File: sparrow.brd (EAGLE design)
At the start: 100 x 100 mm, 189 parts, among them IC1 LAN8720AVIAS, IC2 TLV320AIC3100VIAS, IC3 TPS2500, IC4 SKYWORKS_AAT4280ASC70JW-8-NOT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, IC5 SKYWORKS_AAT4280ASC70JW-8-NOT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, IC6 SKYWORKS_AAT4280ASC70JW-8-NOT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, IC7 SKYWORKS_AAT4280ASC70JW-8-NOT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, IC8 SKYWORKS_AAT4280ASC70JW-8-NOT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, IC9 FXMA10820-DFN, P1 DEBUG, P3 HEADER-1X10ROUND, P4 SD_CARD, X1 ABS07-32768, X2 50MHZ, X3 32.768KHz, Y1 12MHz, Y2 16MHz

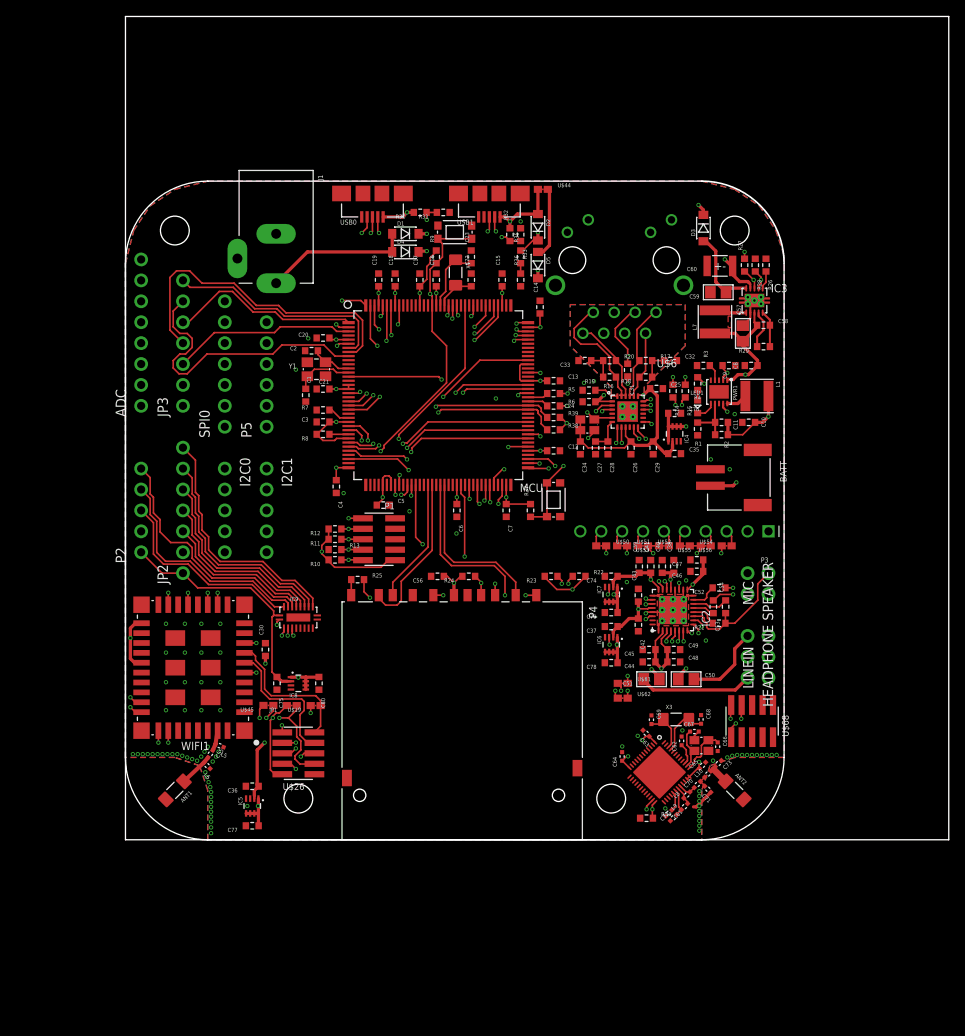
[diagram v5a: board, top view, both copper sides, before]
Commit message: basic routing finished
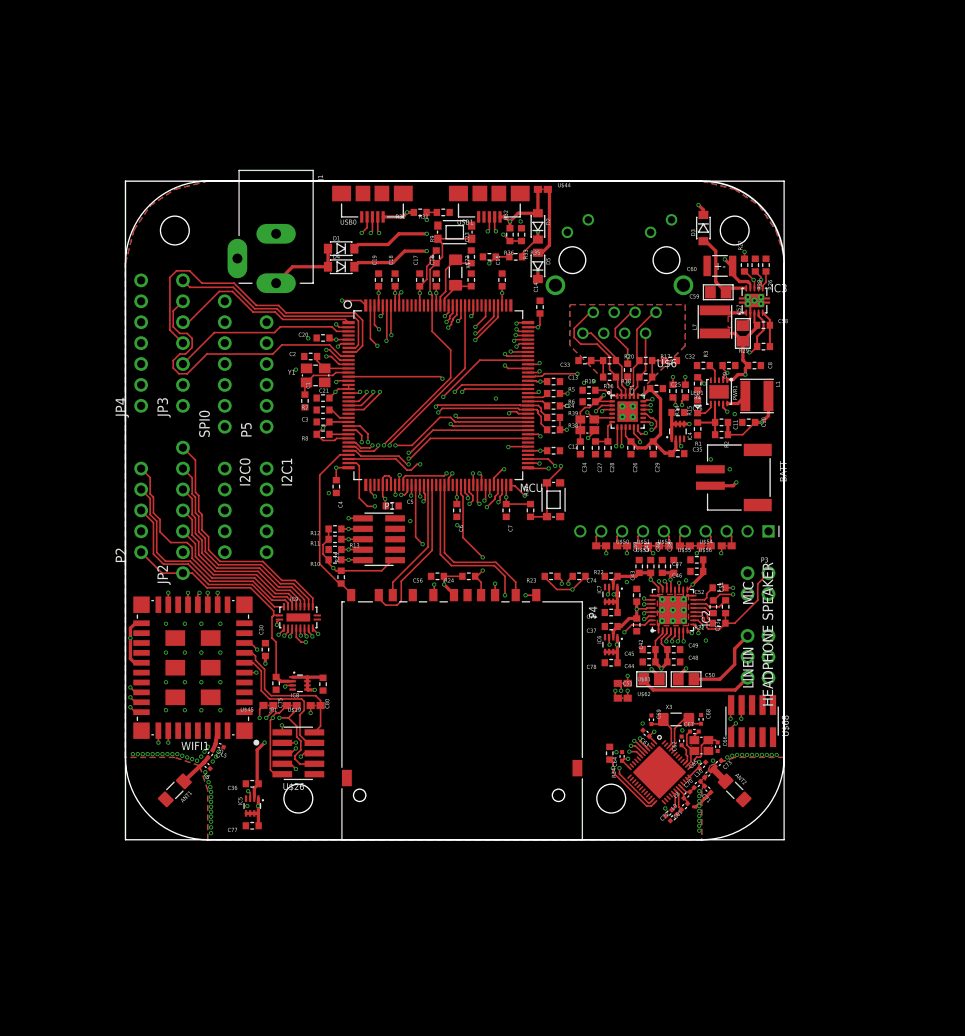
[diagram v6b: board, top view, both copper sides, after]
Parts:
- removed ADC: HEADER-1X8ROUND, anykey:1X08_ROUND
- added JP4: HEADER-1X7ROUND, anykey:1X07_ROUND
- IC3: device anykey:SON10-0.5-EP -> anykey:SON10-0.5-EP-VIAS
- moved R34 9.07 mm to (58.8, 10.5), turned to 270 degrees
- moved D4 8.00 mm to (26.2, 69.6)
- moved D1 8.00 mm to (26.2, 71.8)
- moved R36 4.72 mm to (44.2, 70.8), turned to 0 degrees
- moved R25 2.02 mm to (26.2, 31.9), turned to 90 degrees
- moved C5 1.10 mm to (32.4, 40.5)
- moved C21 1.10 mm to (24.0, 53.6)
- moved Y1 0.76 mm to (23.1, 56.4)
- moved C1 0.71 mm to (21.8, 53.3)
- moved C2 0.71 mm to (22.5, 58.7)
- moved R35 0.60 mm to (47.4, 70.8), turned to 0 degrees
- moved C80 0.51 mm to (24.0, 18.9)
- moved IC4 0.50 mm to (67.1, 49.6)
- moved C76 0.41 mm to (67.1, 51.9)
- moved C8 0.40 mm to (76.4, 57.6), turned to 0 degrees
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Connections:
- removed net ADC7: ADC.8, MCU.136
- new net AVAIL1: MCU.114
- new net AVAIL2: MCU.116
- new net AVAIL6: MCU.117
- new net AVAIL7: MCU.132
- new net AVAIL8: MCU.133
- new net AVAIL9: MCU.134
- net 5V_GEN_EN: now also MCU.95
- net ADC0: now also JP4.1; no longer ADC.1
- net ADC1: now also JP4.2; no longer ADC.2
- net ADC2: now also JP4.3; no longer ADC.3
- net ADC3: now also JP4.4; no longer ADC.4
- net ADC4: now also JP4.5; no longer ADC.5
- net ADC5: now also JP4.6; no longer ADC.6
- net ADC6: now also JP4.7; no longer ADC.7
- net AUDIO_!RESET: now also MCU.121
- net AUDIO_PWR: now also MCU.72
- net ETH_!RST: now also MCU.69
- net ETH_PWR: now also MCU.61
- net GND: now also IC3.EXT1, IC3.EXT2, IC3.EXT3, IC3.EXT4
- net GPIO_1: now also MCU.103
- net GPIO_2: now also MCU.101
- net GPIO_3: now also MCU.100
- net GPIO_4: now also MCU.97
- net GPIO_5: now also MCU.86
- net I2C0_IRQ: now also MCU.11
- net I2C1_IRQ: now also MCU.15
- net NRF_SWDCLK: now also MCU.85
- net NRF_SWDIO: now also MCU.83
- net PORT_PWR_5V: now also MCU.50
- net SD_WP: now also MCU.33
- net SPI0_IRQ: now also MCU.10
- net UART1_CTS: now also MCU1.7
- net UART1_RTS: now also MCU1.6
- net UART1_RXD: now also MCU1.5
- net UART1_TXD: now also MCU1.4
- net V5_IN_SENSE: now also MCU.136
- net WIFI_IRQ: now also MCU.38
- net WIFI_PWR: now also MCU.51
- net WIFI_SW_EN: now also MCU.35
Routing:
- net WIFI_SW_EN: track 0.00 -> 68.5 mm, vias 0 -> 2
- net NRF_SWDCLK: track 25.9 -> 91.9 mm, vias 2 -> 3
- net NRF_SWDIO: track 24.0 -> 85.2 mm, vias 2 -> 3
- net GPIO_1: track 0.00 -> 59.6 mm, vias 0 -> 2
- net AUDIO_!RESET: track 0.00 -> 55.8 mm, vias 0 -> 2
- net GPIO_2: track 0.00 -> 55.6 mm, vias 0 -> 2
- net GPIO_5: track 0.00 -> 55.5 mm, vias 0 -> 2
- net GPIO_3: track 0.00 -> 55.2 mm, vias 0 -> 2
- net GPIO_4: track 0.00 -> 54.4 mm, vias 0 -> 2
- net WIFI_PWR: track 0.00 -> 52.1 mm, vias 0 -> 2
- net UART1_RTS: track 0.00 -> 50.8 mm, vias 0 -> 2
- net ADC7: track 50.6 -> 0.00 mm, vias 1 -> 0
- net UART1_RXD: track 0.00 -> 48.9 mm, vias 0 -> 2
- net UART1_CTS: track 0.00 -> 48.6 mm, vias 0 -> 2
- net UART1_TXD: track 0.00 -> 46.8 mm, vias 0 -> 2
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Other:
- board size 100 x 100 mm -> 80 x 80 mm

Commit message: Silkscreen fixed
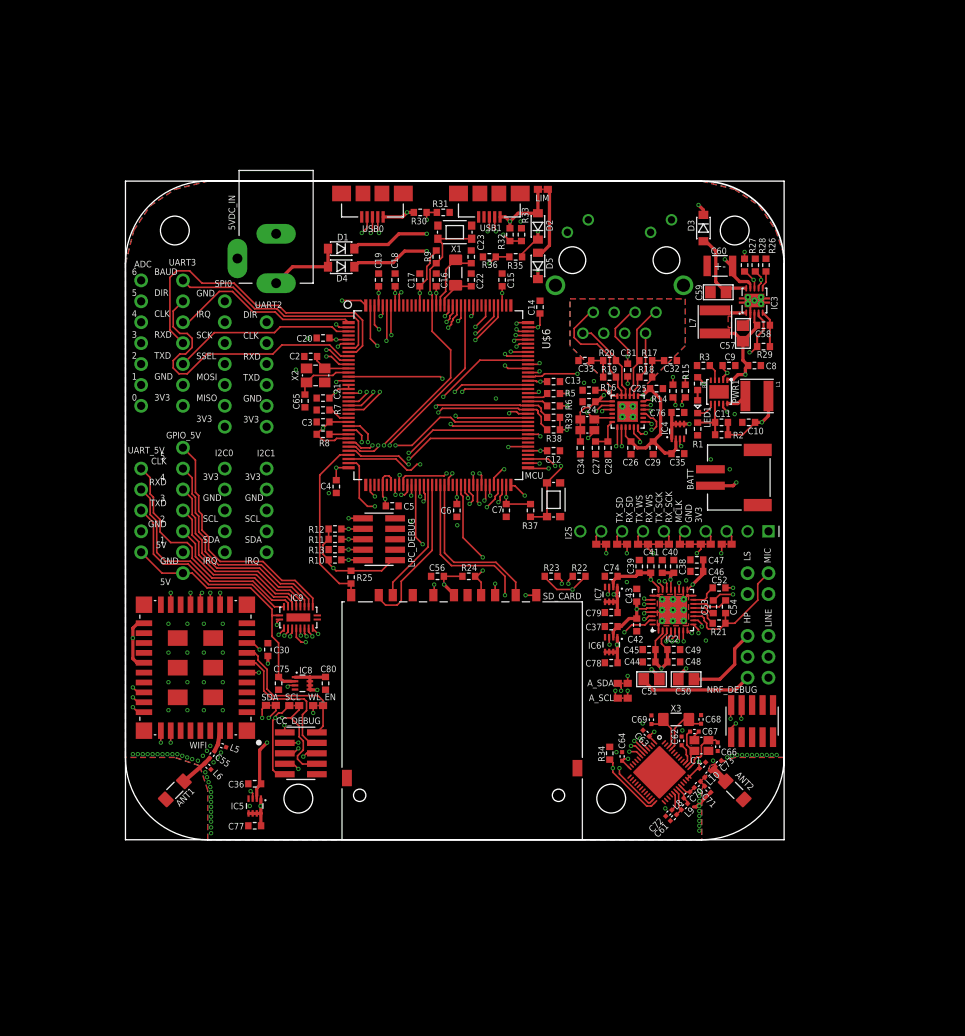
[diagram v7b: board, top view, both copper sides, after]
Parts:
- removed JP1: (no value), anykey:0603_SOLDERJUMPER_CLOSED
- removed U$19, U$45, U$50, U$51, U$52, U$53, U$54, U$55, U$56: JUMPERSOLDER_CLOSED, anykey:0603_SOLDERJUMPER_CLOSED
- removed U$26: HEADER-2X5SMD-1.27MM, anykey:2X05_SMT
- removed WIFI1: CC3000EXTENDED, anykey:CC3000-EXT
- removed Y1: 12MHz, anykey:ABM8G
- added CC_DEBUG: HEADER-2X5SMD-1.27MM, anykey:2X05_SMT
- added LOGO2, LOGO3, LOGO4: LOGOKRONE, anykey:LOGO-KRONE
- added MCLK, RX_SCK, RX_SD, RX_WS, SDA, TX_SCK, TX_SD, TX_WS, WL_EN: JUMPERSOLDER_CLOSED, anykey:0603_SOLDERJUMPER_CLOSED
- added SCL: (no value), anykey:0603_SOLDERJUMPER_CLOSED
- added WIFI: CC3000EXTENDED, anykey:CC3000-EXT
- added X4: 50MHZ, anykey:CRYSTAL25X20
- C1: value 18p -> 1000p; device anykey:0603 -> anykey:0402
- C65: value 1000p -> 18p; device anykey:0402 -> anykey:0603
- X2: value 50MHZ -> 12MHz; device anykey:CRYSTAL25X20 -> anykey:ABM8G
- moved C1 65.5 mm to (70.1, 9.04), turned to 45 degrees
- moved C65 65.5 mm to (21.8, 53.3), turned to 270 degrees
- moved X2 33.5 mm to (23.1, 56.4)
- moved R25 1.20 mm to (27.4, 31.9)
- moved C80 0.32 mm to (24.3, 19.0)
- moved C30 0.30 mm to (17.3, 23.1)
- moved C75 0.30 mm to (18.6, 19.0)
- moved IC8 0.30 mm to (21.5, 19.0)
- moved C36 0.30 mm to (15.7, 6.80)
- moved C77 0.30 mm to (15.7, 1.70)
- moved IC5 0.30 mm to (15.7, 4.10)
- moved L5 0.30 mm to (11.7, 11.4)
- moved C55 0.22 mm to (10.5, 10.3), turned to 235 degrees
- moved L6 0.14 mm to (10.0, 8.92)
- renumbered HEADPHONE to HP, J1 to 5VDC_IN, JP2 to GPIO_5V, JP3 to UART3, JP4 to ADC, LINEIN to LINE, P1 to LPC_DEBUG, P2 to UART_5V, P3 to I2S, P4 to SD_CARD, P5 to UART2, SPEAKER to LS, U$44 to LIM, U$61 to A_SDA, U$62 to A_SCL, U$68 to NRF_DEBUG
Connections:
- net AUDIO_BCLK: now also RX_SCK.2, TX_SCK.2; no longer U$54.2, U$55.2
- net AUDIO_DIN: now also TX_SD.2; no longer U$50.2
- net AUDIO_DOUT: now also RX_SD.2; no longer U$51.2
- net AUDIO_MCLK: now also MCLK.2; no longer U$56.2
- net AUDIO_WCLK: now also RX_WS.2, TX_WS.2; no longer U$52.2, U$53.2
- net ETH_REF_CLK: now also X4.3; no longer X2.3
- net GND: now also C1.P$2, C65.2, CC_DEBUG.10, WIFI.1, WIFI.10, WIFI.11, WIFI.16, WIFI.18, WIFI.20, WIFI.21, WIFI.22, WIFI.25, WIFI.31, WIFI.32, WIFI.33, WIFI.34, WIFI.36, WIFI.37, WIFI.38, WIFI.39, WIFI.40, WIFI.41, WIFI.42, WIFI.43, WIFI.44, WIFI.45, WIFI.46, WIFI.9, X2.4, X4.2; no longer C1.2, C65.P$2, U$26.10, WIFI1.1, WIFI1.10, WIFI1.11, WIFI1.16, WIFI1.18, WIFI1.20, WIFI1.21, WIFI1.22, WIFI1.25, WIFI1.31, WIFI1.32, WIFI1.33, WIFI1.34, WIFI1.36, WIFI1.37, WIFI1.38, WIFI1.39, WIFI1.40, WIFI1.41, WIFI1.42, WIFI1.43, WIFI1.44, WIFI1.45, WIFI1.46, WIFI1.9, Y1.2, Y1.4
- net I2S_RX_MCLK: now also MCLK.1; no longer U$56.1
- net I2S_RX_SCK: now also RX_SCK.1; no longer U$55.1
- net I2S_RX_SD: now also RX_SD.1; no longer U$51.1
- net I2S_RX_WS: now also RX_WS.1; no longer U$53.1
- net I2S_TX_SCK: now also TX_SCK.1; no longer U$54.1
- net I2S_TX_SD: now also TX_SD.1; no longer U$50.1
- net I2S_TX_WS: now also TX_WS.1; no longer U$52.1
- net SPI1_MISO: now also WIFI.13; no longer WIFI1.13
- net SPI1_MOSI: now also WIFI.15; no longer WIFI1.15
- net SPI1_SCK: now also WIFI.17; no longer WIFI1.17
- net SPI1_SSEL: now also WIFI.12; no longer WIFI1.12
- net VD33: now also C1.P$1; no longer C65.P$1
- net VETH33: now also X4.1, X4.4; no longer X2.1, X2.4
- net VWIFI33: now also CC_DEBUG.1, WIFI.19, WIFI.23; no longer U$26.1, WIFI1.19, WIFI1.23
- net WIFI_ANT_UNBAL: now also WIFI.35; no longer WIFI1.35
- net WIFI_IRQ: now also WIFI.14; no longer WIFI1.14
- net WIFI_SCL_CC3000: now also CC_DEBUG.8, SCL.1, WIFI.30; no longer JP1.1, U$26.8, WIFI1.30
- net WIFI_SCL_EEPROM: now also CC_DEBUG.9, SCL.2, WIFI.29; no longer JP1.2, U$26.9, WIFI1.29
- net WIFI_SDA_CC3000: now also CC_DEBUG.6, SDA.1, WIFI.28; no longer U$26.6, U$45.1, WIFI1.28
- net WIFI_SDA_EEPROM: now also CC_DEBUG.7, SDA.2, WIFI.27; no longer U$26.7, U$45.2, WIFI1.27
- net WIFI_SW_EN: now also WIFI.26; no longer WIFI1.26
- net WL_EN1: now also CC_DEBUG.2, WIFI.7, WL_EN.1; no longer U$19.1, U$26.2, WIFI1.7
- net WL_EN2: now also CC_DEBUG.3, WIFI.5, WL_EN.2; no longer U$19.2, U$26.3, WIFI1.5
- net WL_RS232_RX: now also CC_DEBUG.5, WIFI.8; no longer U$26.5, WIFI1.8
- net WL_RS232_TX: now also CC_DEBUG.4, WIFI.6; no longer U$26.4, WIFI1.6
- net XTAL1: now also X2.3; no longer Y1.3
- net XTAL2: now also C65.1, X2.1; no longer C1.1, Y1.1
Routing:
- net V5_OUT: track 221.5 -> 219.6 mm
- net VUSB0: track 54.7 -> 53.3 mm
- net SD_WP: track 20.8 -> 21.5 mm
- net V5_IN: track 85.8 -> 85.2 mm
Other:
- board text added: "3V3 GND SCL SDA IRQ"
- board text added: "5 4 3 2 1 GND 5V"
- board text added: "6 5 4 3 2 1 0"
- board text added: "BAUD DIR CLK RXD TXD GND 3V3"
- board text added: "CLK RXD TXD GND 5V"
- board text added: "DIR CLK RXD TXD GND 3V3"
- board text added: "GND IRQ SCK SSEL MOSI MISO 3V3"
- board text added: "TX_SD RX_SD TX_WS RX_WS TX_SCK RX_SCK MCLK GND 3V3"
- board text added: "^^dkl"

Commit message: power routing, added LEDs, several last-minute improvements
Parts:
- removed C70: 2.2p, anykey:0402
- removed C71, C73: 1p, anykey:0402
- removed L10: 3.3nH, anykey:0402
- removed L8: 4.7nH, anykey:0402
- removed L9: 10nH, anykey:0402
- removed Y2: 16MHz, anykey:CRYSTAL25X20
- added BAL1: BALUNWLCSP, anykey:ST_BAL_WLCSP
- added LED2, LED3, LED4: (no value), anykey:0603_POLAR
- added R40, R41: 33, anykey:0603
- added R42: 10K, anykey:0603
- added R43, R44, R45: 806, anykey:0603
- added X5: 16MHz, anykey:CRYSTAL25X20
- 5VDC_IN: value (none) -> 2A max
- ANT1, ANT2: value (none) -> 2.4GHz 50Ω
- BATT: value (none) -> BATTERY_WITH_HOLDER
- C1: value 1000p -> 1n
- C10, C8, C9: value 4.7u -> 4µ7
- C12, C13, C14, C15, C16, C17, C18, C19, C20, C21, C24, C25, C26, C3, C30, C31, C32, C33, C34, C35, C36, C37, C38, C39, C4, C43, C45, C47, C49, C5, C58, C6, C62, C63, C64, C7, C74, C75: value 0.1µ -> 100n
- C52, C53: value (none) -> 1µ
- C54: value (none) -> 100n
- C55: value (none) -> 2p2
- C61: value 0.047µ -> 47n
- C72: value 2.2p -> 2n2
- D1, D2, D3, D4, D5: value (none) -> MBR230LSFT1
- HP: value (none) -> HP
- I2C0: value (none) -> I2C0
- I2C1: value (none) -> I2C1
- L1: value 10µH -> 10µ
- L5: value (none) -> 2n2
- L6: value (none) -> DNP
- L7: value 2.2µ -> 2µ2
- LIM: value JUMPERSOLDER_CLOSED -> JUMPERSOLDER_OPEN; device anykey:0603_SOLDERJUMPER_CLOSED -> anykey:0603_SOLDERJUMPER_OPEN
- LINE: value (none) -> LINE
- LS: value (none) -> LS
- MIC: value (none) -> MIC
- R2: value 2.4M -> 2M4
- R21: value (none) -> 2K2
- R29, R34: value (none) -> 100K
- SD_CARD: value SD_CARD -> SD_CARDEXTENDED; device anykey:AMPHENOL_101_00313 -> anykey:AMPHENO_101_00313_EXT_PADS
- UART2: value (none) -> UART2
- UART_5V: value (none) -> UART_5V
- X3: value 32.768KHz -> 32768
- moved NRF_DEBUG 16.2 mm to (60.2, 17.3), turned to 90 degrees
- moved X4 16.2 mm to (49.6, 35.6)
- moved C34 14.4 mm to (47.2, 35.6), turned to 90 degrees
- moved C64 9.51 mm to (67.0, 16.9), turned to 0 degrees
- moved C51 7.71 mm to (71.5, 20.8), turned to 0 degrees
- moved C69 7.01 mm to (69.7, 18.5), turned to 180 degrees
- moved C67 6.70 mm to (75.8, 12.9), turned to 90 degrees
- moved A_SDA 6.40 mm to (66.8, 19.0), turned to 90 degrees
- moved R37 6.31 mm to (53.3, 44.8)
- moved C72 6.10 mm to (70.1, 7.68)
- moved C61 5.69 mm to (69.2, 7.94)
- moved A_SCL 5.50 mm to (65.6, 19.0), turned to 90 degrees
- moved C50 5.10 mm to (71.5, 23.3)
- moved C66 5.04 mm to (74.4, 15.7), turned to 0 degrees
- moved C62 4.79 mm to (71.8, 14.3), turned to 45 degrees
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- renumbered U$6 to ETH
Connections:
- net N$19 renamed ETH_LED1_CURR
- net N$20 renamed VUSB1_V5_OUT
- net N$22 renamed ETH_LED2_CURR
- net N$9 renamed CHARGE_!CHRG_CURR
- removed net AVAIL1: MCU.114
- removed net BT_ANT_UNBAL: C70.P$2, C71.P$2, L10.P$1
- removed net ETH_RTERM: C33.1, R19.2, R20.1
- removed net ETH_TTERM: C32.1, R17.2, R18.1
- new net ETH_!INT: IC1.14, MCU.114, R42.1
- new net ETH_REF_CLK_MAC: MCU.45, R40.1
- new net ETH_REF_CLK_PHY: IC1.5, R41.2
- new net N$1: LED2.A, R45.2
- new net N$2: LED3.A, R43.2
- new net N$3: LED4.A, R44.2
- net AVAIL7: now also R45.1
- net AVAIL8: now also R43.1
- net AVAIL9: now also R44.1
- net BT_ANT: now also BAL1.SE; no longer C73.P$2, L10.P$2
- net BT_ANT1: now also BAL1.DIFF2; no longer L8.P$1, L9.P$2
- net BT_ANT2: now also BAL1.DIFF1; no longer C70.P$1, L8.P$2
- net BT_VDD_PA: now also BAL1.VCC; no longer L9.P$1
- net BT_XC1: now also C67.P$1, X5.1; no longer C66.P$1, Y2.3
- net BT_XC2: now also C66.P$1, X5.3; no longer C67.P$1, Y2.1
- net ETH_REF_CLK: now also R40.2, R41.1; no longer IC1.5, MCU.45
- net GND: now also BAL1.GND, BATT.3, BATT.4, LED2.K, LED3.K, LED4.K, MCU1.13, MCU1.33, MCU1.34, MCU1.PAD, X5.2, X5.4; no longer C71.P$1, C73.P$1, Y2.2, Y2.4
- net VETH33: now also C32.1, C33.1, R17.2, R18.1, R19.2, R20.1, R42.2
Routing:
- net VD33: track 119.8 -> 595.4 mm, vias 30 -> 32
- net ETH_!INT: track 0.00 -> 37.6 mm, vias 0 -> 3
- net ETH_REF_CLK: track 30.6 -> 3.25 mm, vias 2 -> 0
- net GND: track 37.8 -> 57.5 mm, vias 91 -> 116
- net NRF_SWDCLK: track 91.9 -> 72.8 mm, vias 3 -> 2
- net ETH_REF_CLK_PHY: track 0.00 -> 17.3 mm
- net ETH_REF_CLK_MAC: track 0.00 -> 17.2 mm, vias 0 -> 2
- net NRF_SWDIO: track 85.2 -> 68.4 mm, vias 3 -> 2
- net USB0_PWR_FAULT: track 63.4 -> 51.7 mm
- net USB0_PPWR: track 62.0 -> 51.2 mm
- net HP_R: track 13.9 -> 3.58 mm
- net VETH33: track 85.7 -> 95.8 mm, vias 4 -> 5
- net AVAIL7: track 0.00 -> 8.02 mm
- net VPOWER: track 9.33 -> 16.8 mm
- net ETH_LED1_CURR: track 33.1 -> 26.4 mm
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- added copper zone on layer 15, net VETH33
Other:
- board text added: "GND cutout to separate GND from PGND. See schematics notes."
